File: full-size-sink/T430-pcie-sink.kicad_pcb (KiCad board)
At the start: 2 copper layers, 30 x 51 mm, 23 parts, among them J1 miniPCIe, J10 Conn_01x01, J11 Conn_01x01, J12 Conn_01x01, J13 Conn_01x01, J14 Conn_01x01, J15 Conn_01x01, J2 Conn_01x22_MountingPin, J3 Conn_01x24_MountingPin, J4 M.2-NGFF-A+E-Key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

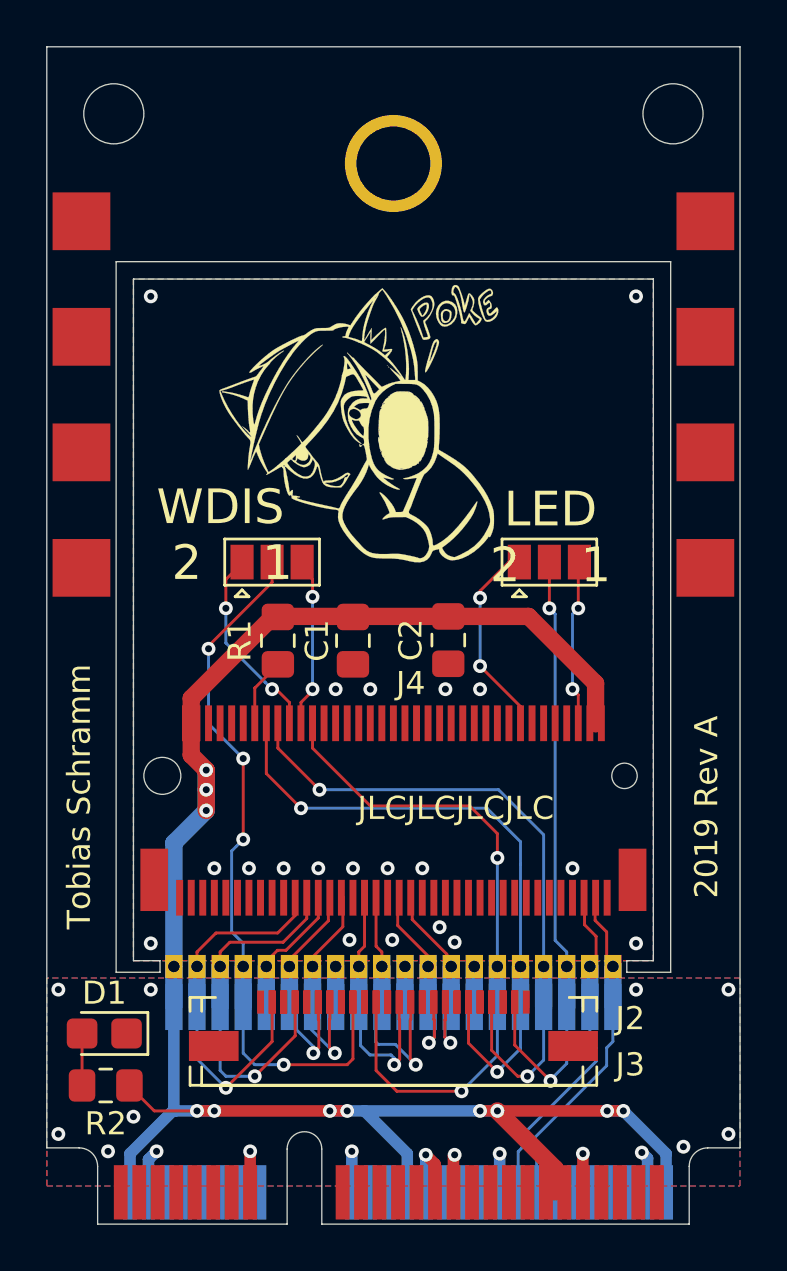
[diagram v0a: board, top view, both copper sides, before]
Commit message: Add suspend oscillator
Seems to be mandatory in the NGFF M.2 spec
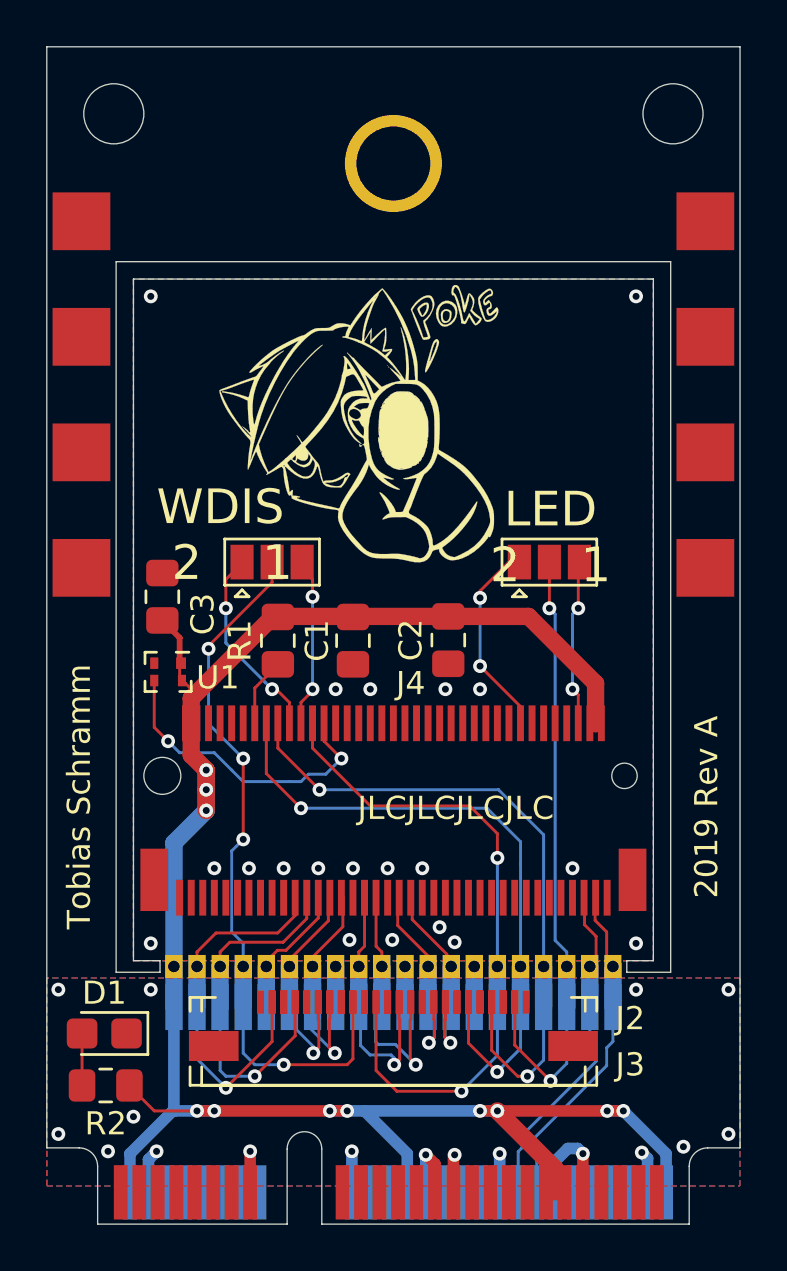
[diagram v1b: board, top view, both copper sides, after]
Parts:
- added C3: 100 nC, Capacitor_SMD:C_0805_2012Metric_Pad1.15x1.40mm_HandSolder, F.Cu at (25.0, 43.8)
- added U1: DSC60XXB, microchip-lga:LGA4-1.6x1.2, F.Cu at (25.2, 47.0)
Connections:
- J4 pad 50: Net-(J4-Pad50) -> /SUSCLK
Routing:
- net /SUSCLK: track 0.00 -> 13.3 mm, vias 0 -> 2
- net +3V3: track 85.9 -> 89.5 mm
- net GND: track 26.8 -> 29.7 mm
